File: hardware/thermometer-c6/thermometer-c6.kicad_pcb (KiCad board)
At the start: 2 copper layers, 48 x 35 mm, 101 parts, among them J1 JST-PH-2 BAT, J2 MEAS_HDR, J3 USB-C, J4 EPD FPC24 0.5mm, J5 DEBUG, Q1 AO3401A, Q2 AO3401A, Q3 Si1308EDL, Q4 AO3401A, Q5 2N7002, Q6 AO3401A, SW1 RESET, SW2 BOOT, U1 ESP32-C6-MINI-1-N4, U2 RT9080-33GJ5, U3 USBLC6-2SC6, U4 MCP73831-2, U5 BMP581, U6 BMP585, Y1 32.768kHz FC-135

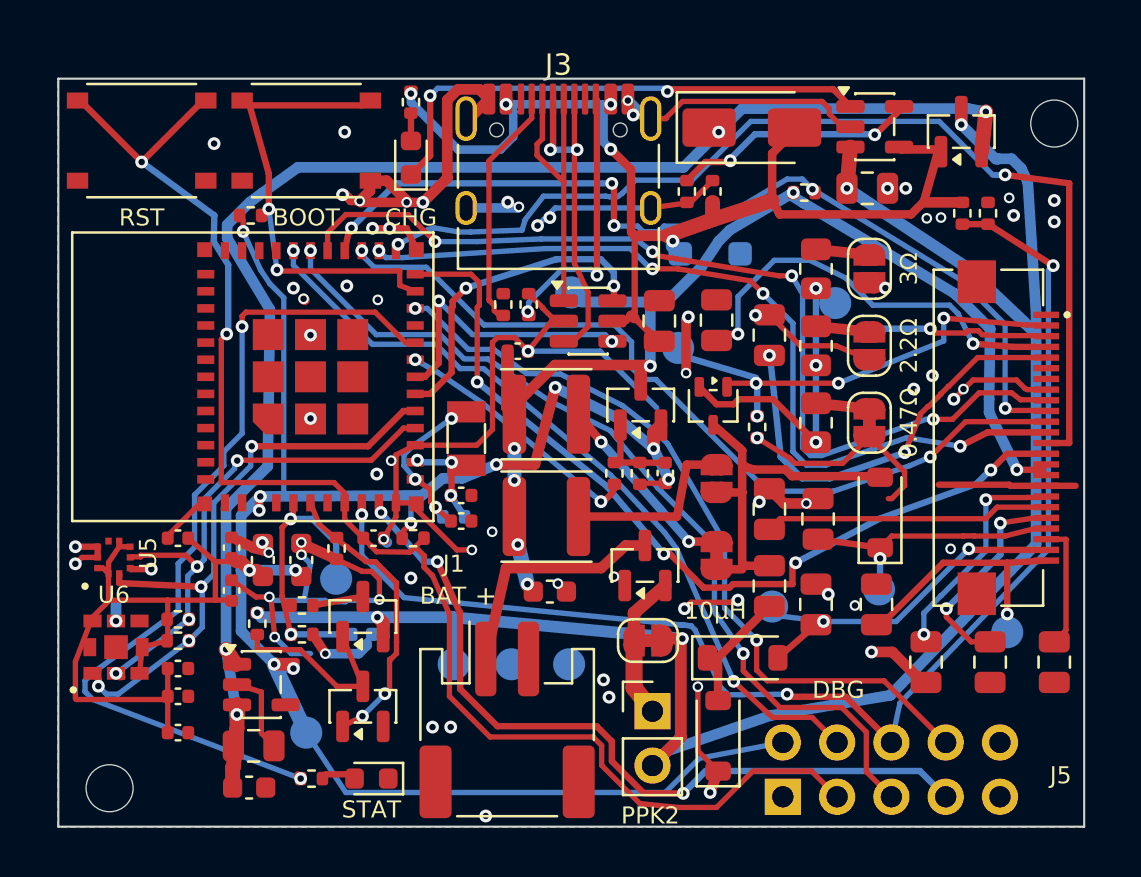
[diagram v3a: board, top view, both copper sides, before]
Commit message: Promote C29 to populated front-side part; M7 silk polish batch
C29 (10nF ADC reservoir): back DNP -> front populated at (12.6,27.7), dnp=False + LCSC C15195, routed (harvested from GUI). Netlist/pin-set unchanged; invariants desc, README, EE-PRIMER, BOM regenerated. Silk batch: 47uH value by JP6 (user spot 27.8,20.0); FPC pin 1/24 markers on J4; 'fit ONE'->'U5/U6 fit ONE'; bridge legend split to 3 spaced lines; 'CHARGE INDOORS 0-45C' contiguous; R9 10M label cleared of VBAT_ADC; TP4->'3V3 probe-only'; '3.7V LiPo' by J1 (on back - no front room); board name -> 'Low-Power E-Paper Thermometer  rev A'; looser back-silk line spacing; corrected C9/C14/C15 floorplan comment. Gate: 0 unconnected, 0 DRC (silk incl text-size all 0), check_pcb OK, make check green, byte-stable.

Co-Authored-By: Claude Opus 4.8 (1M context) <noreply@anthropic.com>
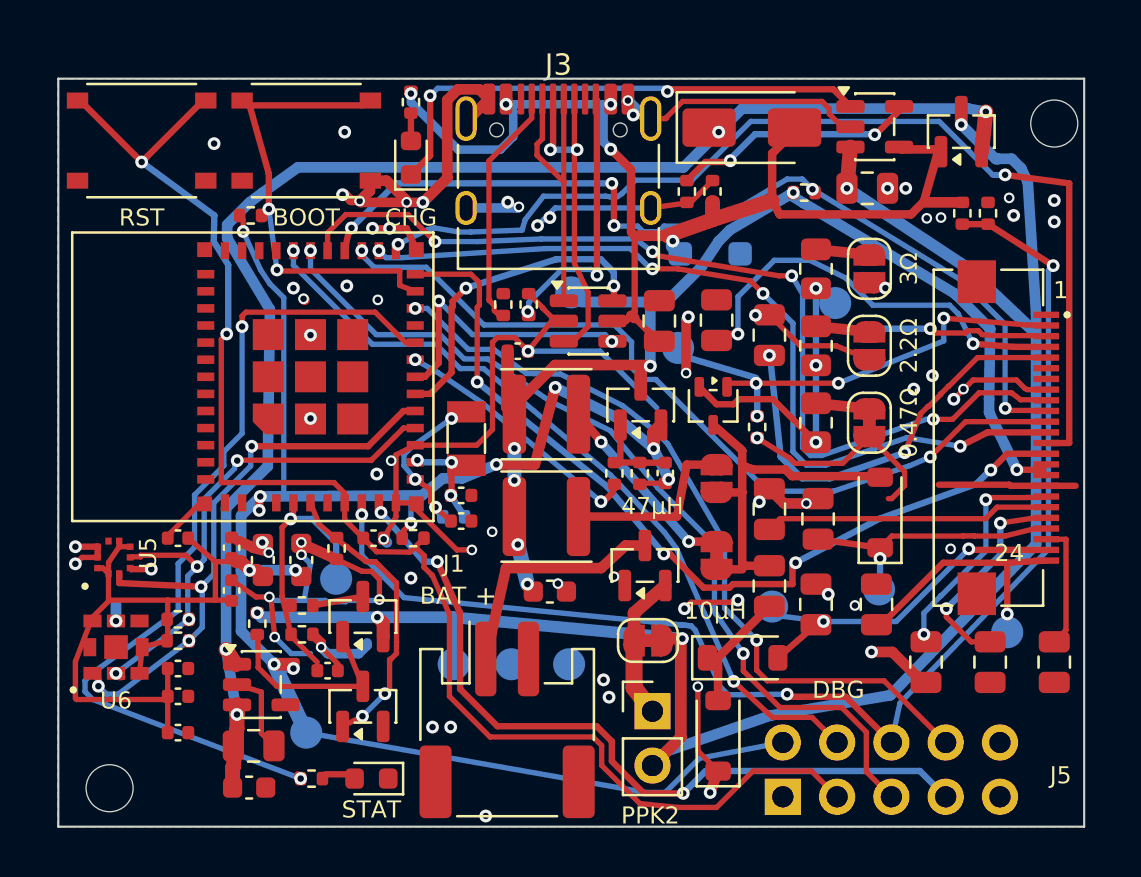
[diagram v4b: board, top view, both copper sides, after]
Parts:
- C29: moved to F.Cu
- moved C29 2.33 mm to (112.6, 127.7)
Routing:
- net GND: track 150.9 -> 152.3 mm
- net +3V3: track 115.1 -> 113.9 mm
- net VBAT_ADC: track 13.5 -> 12.5 mm, vias 2 -> 1
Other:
- board text added: "1"
- board text added: "24"
- board text added: "3.7V LiPo"
- board text added: "3V3 probe-only"
- board text added: "47µH"
- board text added: "CHARGE INDOORS 0-45°C"
- board text added: "D7 SMF5.0A"
- board text added: "IND 10/47µH = JP5/6"
- board text added: "Low-Power E-Paper"
- board text added: "R9 10M"
- board text added: "RESE 0.47/2.2/3Ω = JP2/3/4"
- board text added: "Thermometer rev A"
- board text added: "U5/U6 fit ONE"
- board text added: "bridge ONE"
- board text removed: "0-45°C"
- board text removed: "3V3"
- board text removed: "CHARGE INDOORS"
- board text removed: "bridge ONE RESE 0.47/2.2/3Ω=JP2/3/4 IND 10/47µH=JP5/6"
- board text removed: "fit ONE"
- board text removed: "thermometer-c6 rev A"

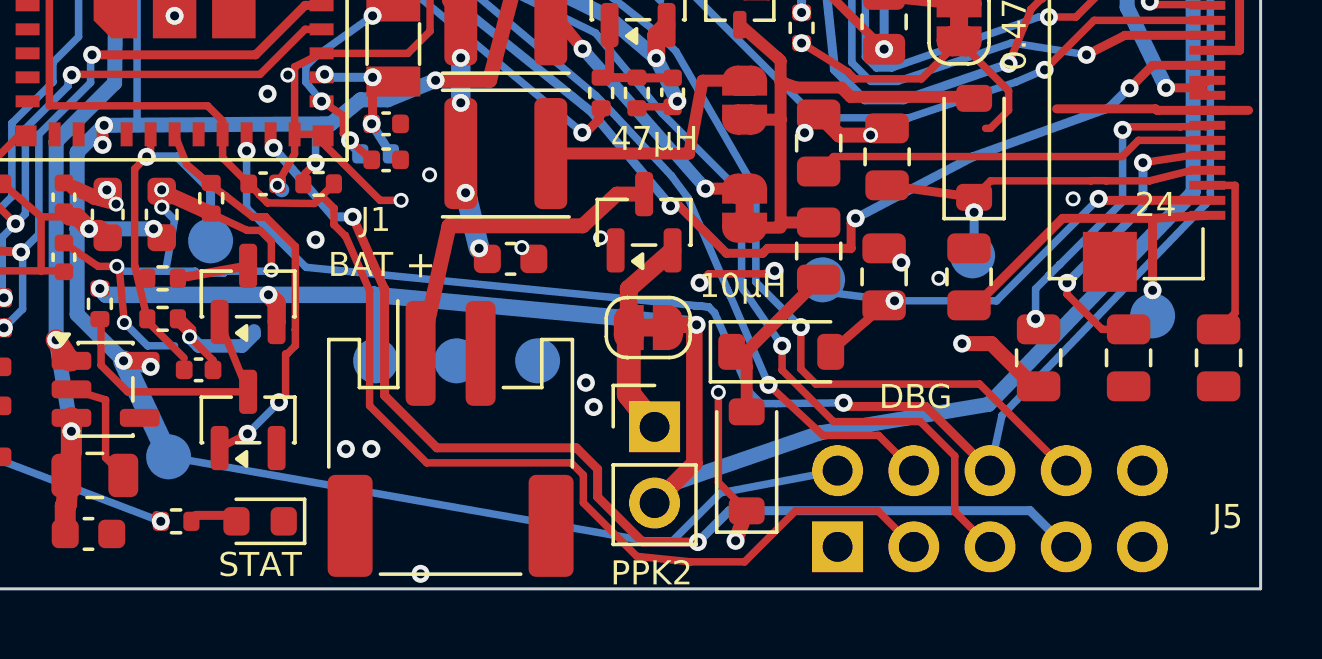
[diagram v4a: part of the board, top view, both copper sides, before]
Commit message: M7: silk refinements + antenna keep-out outline (IBAT/STATUS, DBG+J5, name, bridge block)
Board name hyphens dropped (Low Power ePaper Thermometer, stroke font rendered '-' wide). bridge-ONE/values/fit-ONE gathered into one left-aligned NE back block, keyed off component values not JP refdes (JPs aren't on silk). Front DBG+J5 grouped. FPC '24' removed (under J4 body), '1' kept. PPK2->IBAT (battery-current break; REQUIRED_SILK + README updated, PPK2 kept as recommended meter). STAT->STATUS. Antenna keep-out (0,7.25,5.3,20.65) outlined on B.SilkS + 'ANTENNA KEEP CLEAR' note (front is under U1 module; back is bare + RF-safe). New generator: add_silk_shapes / SILK_SHAPES (rect+line PCB_SHAPE on silk). Gate: 0 DRC/unconnected, check_pcb OK, make check green, byte-stable.

Co-Authored-By: Claude Opus 4.8 (1M context) <noreply@anthropic.com>
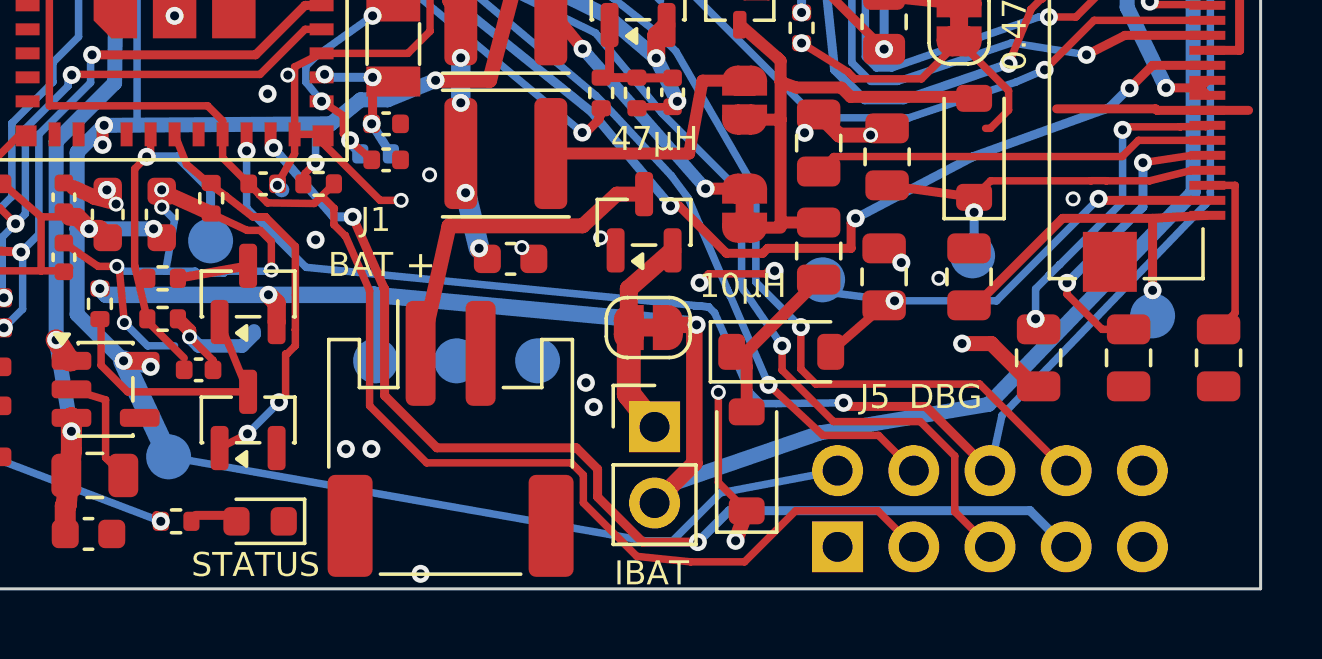
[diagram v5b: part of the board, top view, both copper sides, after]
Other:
- board text added: "ANTENNA"
- board text added: "IBAT"
- board text added: "IND 10/47µH"
- board text added: "KEEP CLEAR"
- board text added: "Low Power ePaper"
- board text added: "RESE 0.47/2.2/3Ω"
- board text added: "STATUS"
- board text added: "bridge ONE:"
- board text removed: "24"
- board text removed: "IND 10/47µH = JP5/6"
- board text removed: "Low-Power E-Paper"
- board text removed: "PPK2"
- board text removed: "RESE 0.47/2.2/3Ω = JP2/3/4"
- board text removed: "STAT"
- board text removed: "bridge ONE"
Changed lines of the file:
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@@
 		(layer "Edge.Cuts")
 	)
+	(gr_rect
+		(start 100.5 107.25)
+		(end 105.3 120.65)
+		(stroke
+			(width 0.15)
+			(type default)
+		)
+		(fill no)
+		(layer "B.SilkS")
+	)
 	(gr_text "+"
 		(at 120 124.2 0)
@@
 		)
 	)
-	(gr_text "24"
-		(at 144.5 122.2 0)
-		(layer "F.SilkS")
-		(effects
-			(font
-				(size 0.8 0.8)
-				(thickness 0.15)
-			)
-		)
-	)
 	(gr_text "3.7V LiPo"
 		(at 120.8 131.199999 0)
@@
 		)
 	)
+	(gr_text "ANTENNA"
+		(at 102 113.95 90)
+		(layer "B.SilkS")
+		(effects
+			(font
+				(size 0.8 0.8)
+				(thickness 0.15)
+			)
+			(justify mirror)
+		)
+	)
 	(gr_text "BAT"
 		(at 118 124.2 0)
@@
 	)
 	(gr_text "DBG"
-		(at 136.5 128.6 0)
+		(at 137.5 128.6 0)
 		(layer "F.SilkS")
 		(effects
@@
 		)
 	)
-	(gr_text "IND 10/47µH = JP5/6"
-		(at 114.73 118.4 0)
+	(gr_text "IBAT"
+		(at 127.7 134.48 0)
+		(layer "F.SilkS")
+		(effects
+			(font
+				(size 0.8 0.8)
+				(thickness 0.15)
+			)
+		)
+	)
+	(gr_text "IND 10/47µH"
+		(at 136.74 104.8 0)
 		(layer "B.SilkS")
 		(effects
@@
 		)
 	)
-	(gr_text "Low-Power E-Paper"
-		(at 107.395 101.3 0)
+	(gr_text "KEEP CLEAR"
+		(at 103.6 113.95 90)
 		(layer "B.SilkS")
 		(effects
@@
 		)
 	)
-	(gr_text "MOUNT TOP"
-		(at 139 126.9 0)
+	(gr_text "Low Power ePaper"
+		(at 106.69 101.3 0)
 		(layer "B.SilkS")
 		(effects
@@
 		)
 	)
-	(gr_text "PPK2"
-		(at 127.7 134.48 0)
-		(layer "F.SilkS")
+	(gr_text "MOUNT TOP"
+		(at 139 126.9 0)
+		(layer "B.SilkS")
 		(effects
 			(font
@@
 				(thickness 0.15)
 			)
+			(justify mirror)
 		)
 	)
@@
 		)
 	)
-	(gr_text "RESE 0.47/2.2/3Ω = JP2/3/4"
-		(at 117.205 117 0)
+	(gr_text "RESE 0.47/2.2/3Ω"
+		(at 138.42 103.4 0)
 		(layer "B.SilkS")
 		(effects
@@
 		)
 	)
-	(gr_text "STAT"
-		(at 114.65 134.199999 0)
+	(gr_text "STATUS"
+		(at 114.5 134.199999 0)
 		(layer "F.SilkS")
 		(effects
@@
 	)
 	(gr_text "U5/U6 fit ONE"
-		(at 105 124.3 0)
+		(at 137.12 106.2 0)
 		(layer "B.SilkS")
 		(effects
@@
 		)
 	)
-	(gr_text "bridge ONE"
-		(at 111.015 115.6 0)
+	(gr_text "bridge ONE:"
+		(at 136.21 102 0)
 		(layer "B.SilkS")
 		(effects
@@
 		(tags "Through hole pin header THT 2x05 2.54mm double row")
 		(property "Reference" "J5"
-			(at 1 13 0)
+			(at 5 1.25 0)
 			(layer "F.SilkS")
 			(effects

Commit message: Harvest GUI silk reorg (2 corner info blocks) + trace tweaks; add silk justification
Wholesale-harvested out/hand authored silk (44 texts, 44/44 fidelity). Consolidated notes into two native multi-line blocks: NW github/name/rev/CHARGE-INDOORS (top-anchored), NE 'EPD: bridge one only / RESE.. / IND.. / Sensor: fit one only / U5 BMP581 U6 BMP585' (top-anchored, edge-justified). add_silk gains optional H/V justify (SetHorizJustify/SetVertJustify, non-default only). FPC pin-24 as stacked 2/4; moved J5/GND/3.7V LiPo; U5 refdes moved. J3 dropped from KEEP_SILK_REFS -> F.Fab (was off the north edge). GND stitch via (13.4,2.5)->(14.9,2.5); BOOT/VBAT trace tweaks harvested. check_pcb REQUIRED_SILK lowercased (bridge one/fit one). Grammar separator = colon (stroke-font dash renders wide). Gate: 0 DRC/unconnected, check_pcb OK, make check green, byte-stable.

Co-Authored-By: Claude Opus 4.8 (1M context) <noreply@anthropic.com>
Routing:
- net BOOT: track 20.8 -> 21.9 mm
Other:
- board text added: "2 4"
- board text added: "EPD: bridge one only RESE 0.47/2.2/3Ω IND 10/47µH Sensor: fit one only U5 BMP581/U6 BMP585"
- board text added: "github.com/antoinecellerier Low Power ePaper Thermometer rev A CHARGE INDOORS 0-45°C"
- board text removed: "CHARGE INDOORS 0-45°C"
- board text removed: "IND 10/47µH"
- board text removed: "Low Power ePaper"
- board text removed: "RESE 0.47/2.2/3Ω"
- board text removed: "Thermometer rev A"
- board text removed: "U5/U6 fit ONE"
- board text removed: "bridge ONE:"
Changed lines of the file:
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@@
 		)
 	)
+	(gr_text "2\n4"
+		(at 147 124.4 0)
+		(layer "F.SilkS")
+		(effects
+			(font
+				(size 0.8 0.8)
+				(thickness 0.15)
+			)
+		)
+	)
 	(gr_text "3.7V LiPo"
-		(at 120.8 131.199999 0)
+		(at 121 133.9 0)
 		(layer "B.SilkS")
 		(effects
@@
 		)
 	)
-	(gr_text "CHARGE INDOORS 0-45°C"
-		(at 109.05 104.1 0)
-		(layer "B.SilkS")
-		(effects
-			(font
-				(size 0.8 0.8)
-				(thickness 0.15)
-			)
-			(justify mirror)
-		)
-	)
 	(gr_text "CHG"
 		(at 116.5 106.5 0)
@@
 		)
 	)
+	(gr_text "EPD: bridge one only\nRESE 0.47/2.2/3Ω\nIND 10/47µH\nSensor: fit one only\nU5 BMP581/U6 BMP585"
+		(at 144 100.6 0)
+		(layer "B.SilkS")
+		(effects
+			(font
+				(size 0.8 0.8)
+				(thickness 0.15)
+			)
+			(justify left top mirror)
+		)
+	)
 	(gr_text "EPD_VCC"
 		(at 124 111.9 0)
@@
 	)
 	(gr_text "GND"
-		(at 121.2 125.7 0)
+		(at 121.2 129.3 0)
 		(layer "B.SilkS")
 		(effects
@@
 		)
 	)
-	(gr_text "IND 10/47µH"
-		(at 136.74 104.8 0)
-		(layer "B.SilkS")
-		(effects
-			(font
-				(size 0.8 0.8)
-				(thickness 0.15)
-			)
-			(justify mirror)
-		)
-	)
 	(gr_text "IO4"
 		(at 138.98 128.15 0)
@@
 	)
 	(gr_text "J5"
-		(at 131.199999 128.75 0)
+		(at 146.7 132.1 0)
 		(layer "B.SilkS")
 		(effects
@@
 		)
 	)
-	(gr_text "Low Power ePaper"
-		(at 106.69 101.3 0)
-		(layer "B.SilkS")
-		(effects
-			(font
-				(size 0.8 0.8)
-				(thickness 0.15)
-			)
-			(justify mirror)
-		)
-	)
 	(gr_text "MOUNT TOP"
 		(at 139 126.9 0)
@@
 		)
 	)
-	(gr_text "RESE 0.47/2.2/3Ω"
-		(at 138.42 103.4 0)
-		(layer "B.SilkS")
-		(effects
-			(font
-				(size 0.8 0.8)
-				(thickness 0.15)
-			)
-			(justify mirror)
-		)
-	)
 	(gr_text "RESE"
 		(at 136.35 112.3 0)
@@
 		)
 	)
-	(gr_text "Thermometer   rev A"
-		(at 107.45 102.7 0)
-		(layer "B.SilkS")
-		(effects
-			(font
-				(size 0.8 0.8)
-				(thickness 0.15)
-			)
-			(justify mirror)
-		)
-	)
-	(gr_text "U5/U6 fit ONE"
-		(at 137.12 106.2 0)
-		(layer "B.SilkS")
-		(effects
-			(font
-				(size 0.8 0.8)
-				(thickness 0.15)
-			)
-			(justify mirror)
-		)
-	)
 	(gr_text "VBAT"
 		(at 118.5 125.7 0)
@@
 		)
 	)
-	(gr_text "bridge ONE:"
-		(at 136.21 102 0)
+	(gr_text "github.com/antoinecellerier\n\nLow Power ePaper Thermometer\nrev A\nCHARGE INDOORS 0-45°C"
+		(at 101 100.6 0)
 		(layer "B.SilkS")
 		(effects
@@
 				(thickness 0.15)
 			)
-			(justify mirror)
+			(justify right top mirror)
 		)
 	)
@@
 		(property "Reference" "J3"
 			(at 0 -5.645 0)
-			(layer "F.SilkS")
+			(layer "F.Fab")
 			(effects
 				(font
@@
 		(tags "LGA BMP581 Bosch")
 		(property "Reference" "U5"
-			(at 0.2 1.6 90)
+			(at -0.5 2.1 180)
 			(layer "F.SilkS")
 			(effects
@@
 	)
 	(segment
+		(start 102.85 121.9)
+		(end 103.362 121.9)
+		(width 0.25)
+		(layer "F.Cu")
+		(net "+3V3")
+	)
+	(segment
 		(start 102.85 123.162)
 		(end 102.85 123.6)
@@
 	)
 	(segment
-		(start 103.362 121.9)
-		(end 102.85 121.9)
-		(width 0.25)
-		(layer "F.Cu")
-		(net "+3V3")
-	)
-	(segment
 		(start 103.412 122.95)
 		(end 103.362 122.9)
@@
 	)
 	(segment
-		(start 105.12 128.9)
-		(end 104.97 129.05)
+		(start 105.12 127.6)
+		(end 105.12 128.9)
 		(width 0.25)
 		(layer "F.Cu")
@@
 	(segment
 		(start 105.12 128.9)
-		(end 105.12 127.6)
+		(end 104.97 129.05)
 		(width 0.25)
 		(layer "F.Cu")
@@
 	(segment
 		(start 107.35 122.6)
-		(end 108.3 122.6)
-		(width 0.25)
-		(layer "F.Cu")
-		(net "+3V3")
-	)
-	(segment
-		(start 107.35 124.4)
-		(end 107.35 122.6)
+		(end 107.35 124.4)
 		(width 0.25)
 		(layer "F.Cu")
@@
 	(segment
 		(start 108.3 122.6)
+		(end 107.35 122.6)
+		(width 0.25)
+		(layer "F.Cu")
+		(net "+3V3")
+	)
+	(segment
+		(start 108.3 122.6)
 		(end 108.55 122.6)
 		(width 0.6)
@@
 	)
 	(segment
+		(start 108.6 101.025)
+		(end 111.562 103.987)
+		(width 0.3)
+		(layer "F.Cu")
+		(net "BOOT")
+	)
+	(segment
 		(start 108.6 111.105)
 		(end 108.78 110.925)
@@
 	)
 	(segment
-		(start 108.95 101.25)
-		(end 109.85 104.45)
-		(width 0.3)
-		(layer "F.Cu")
-		(net "BOOT")
-	)
-	(segment
 		(start 108.95 105.789)
 		(end 107.9 106.839)
@@
 	)
 	(segment
-		(start 109.85 104.45)
+		(start 109.85 105.775)
 		(end 109.85 106.1)
 		(width 0.3)
@@
 	)
 	(segment
+		(start 111.562 103.987)
+		(end 111.562 104.062)
+		(width 0.3)
+		(layer "F.Cu")
+		(net "BOOT")
+	)
+	(segment
 		(start 111.6 130.6)
 		(end 110.1 127.4)
@@
 	)
 	(segment
-		(start 114.25 101.25)
-		(end 108.95 101.25)
-		(width 0.3)
-		(layer "F.Cu")
-		(net "BOOT")
-	)
-	(segment
 		(start 114.25 128.433)
 		(end 113.3 126.108)
@@
 	)
 	(segment
+		(start 114.6 101.025)
+		(end 109.85 105.775)
+		(width 0.3)
+		(layer "F.Cu")
+		(net "BOOT")
+	)
+	(segment
 		(start 114.6 104.775)
 		(end 115.361 104.775)
@@
 	)
 	(segment
+		(start 114.6 122.6)
+		(end 114.836 122.6)
+		(width 0.25)
+		(layer "F.Cu")
+		(net "VDIV_EN")
+	)
+	(segment
 		(start 114.625 121.855)
 		(end 113.4 120.63)
@@
 	(segment
 		(start 114.836 122.6)
-		(end 114.6 122.6)
-		(width 0.25)
-		(layer "F.Cu")
-		(net "VDIV_EN")
-	)
-	(segment
-		(start 114.836 122.6)
 		(end 115.826 123.59)
 		(width 0.25)
@@
 	)
 	(segment
+		(start 130.61 106.6)
+		(end 133.4 105.7)
+		(width 0.7)
+		(layer "F.Cu")
+		(net "VBUS")
+	)
+	(segment
 		(start 130.639999 116.198)
 		(end 131.9 117.3)
@@
 	(segment
 		(start 133.4 105.7)
-		(end 130.61 106.6)
-		(width 0.7)
-		(layer "F.Cu")
-		(net "VBUS")
-	)
-	(segment
-		(start 133.4 105.7)
 		(end 133.75 106.35)
 		(width 0.4)
@@
 	)
 	(segment
-		(start 135.45 110.05)
-		(end 135.45 111.7)
-		(width 0.3)
-		(layer "B.Cu")
-		(net "EPD_RESE")
-	)
-	(segment
 		(start 135.45 111.588)
 		(end 137.95 111.85)
@@
 	(segment
 		(start 135.45 111.7)
+		(end 135.45 110.05)
+		(width 0.3)
+		(layer "B.Cu")
+		(net "EPD_RESE")
+	)
+	(segment
+		(start 135.45 111.7)
 		(end 140.8 111.7)
 		(width 0.3)
@@
 	(segment
 		(start 142.25 102.15)
-		(end 143.863 103.763)
+		(end 144.78 103.919)
 		(width 0.5)
 		(layer "B.Cu")
@@
 	)
 	(segment
-		(start 143.863 103.763)
-		(end 143.976 103.763)
-		(width 0.5)
-		(layer "B.Cu")
-		(net "VBAT")
-	)
-	(segment
 		(start 143.927 120.05)
 		(end 146.225 120.05)
@@
 	)
 	(segment
-		(start 143.976 103.763)
-		(end 143.989 103.75)
-		(width 0.5)
-		(layer "B.Cu")
-		(net "VBAT")
-	)
-	(segment
-		(start 143.989 103.75)
-		(end 144.611 103.75)
-		(width 0.5)
-		(layer "B.Cu")
-		(net "VBAT")
-	)
-	(segment
 		(start 144.078 120.795)
 		(end 144.078 122.271999)
@@
 	(segment
 		(start 144.4 122.65)
-		(end 144.4 125.05)
+		(end 146.225 122.55)
 		(width 0.3)
 		(layer "F.Cu")
@@
 	)
 	(segment
-		(start 144.4 122.65)
-		(end 146.225 122.55)
+		(start 144.4 125.05)
+		(end 144.4 122.65)
 		(width 0.3)
 		(layer "F.Cu")
@@
 	)
 	(segment
-		(start 144.611 103.75)
-		(end 145.05 104.189)
-		(width 0.5)
-		(layer "B.Cu")
-		(net "VBAT")
-	)
-	(segment
 		(start 144.695 112.55)
 		(end 145.7 112.55)
@@
 	)
 	(segment
+		(start 144.78 103.919)
+		(end 145.05 104.189)
+		(width 0.5)
+		(layer "B.Cu")
+		(net "VBAT")
+	)
+	(segment
 		(start 144.832 114.1)
 		(end 142.8 114.1)
@@
 	)
 	(via
-		(at 113.4 102.5)
-		(size 0.6)
-		(drill 0.3)
-		(layers "F.Cu" "B.Cu")
-		(net "GND")
-	)
-	(via
 		(at 113.5 109.7)
 		(size 0.6)
@@
 		(size 0.6)
 		(drill 0.3)
+		(layers "F.Cu" "B.Cu")
+		(net "GND")
+	)
+	(via
+		(at 114.9 102.5)
+		(size 0.6)
+		(drill 0.3)
